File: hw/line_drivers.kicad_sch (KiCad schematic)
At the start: 0 parts

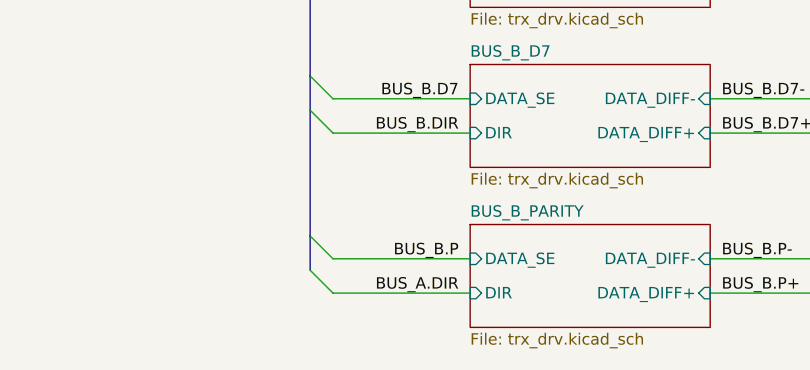
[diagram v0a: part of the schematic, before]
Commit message: BUS*B* Parity bit driver direction pin was accidentally connected to BUS*A* direction net
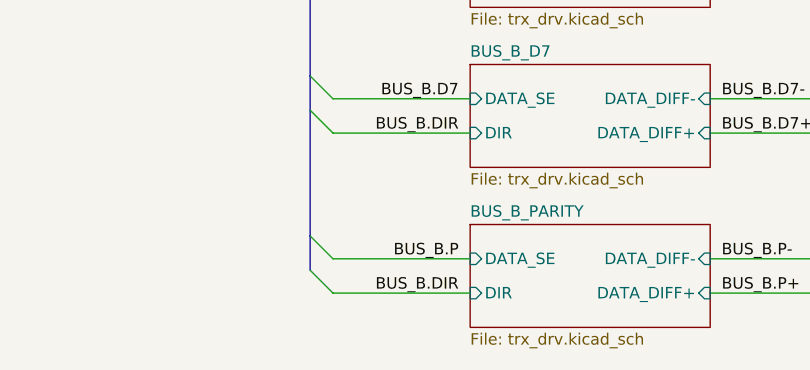
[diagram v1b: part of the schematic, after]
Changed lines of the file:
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@@
     (effects (font (size 1.27 1.27)) (justify right bottom))
   )
-  (label "BUS_A.DIR" (at 194.31 213.36 180) (fields_autoplaced)
+  (label "BUS_B.DIR" (at 194.31 213.36 180) (fields_autoplaced)
     (effects (font (size 1.27 1.27)) (justify right bottom))
   )
